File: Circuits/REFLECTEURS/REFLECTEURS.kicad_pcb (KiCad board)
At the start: 2 copper layers, 118.4 x 31 mm, 24 parts, among them P1 HE10-10, U1 3mm_hole, U2 3mm_hole

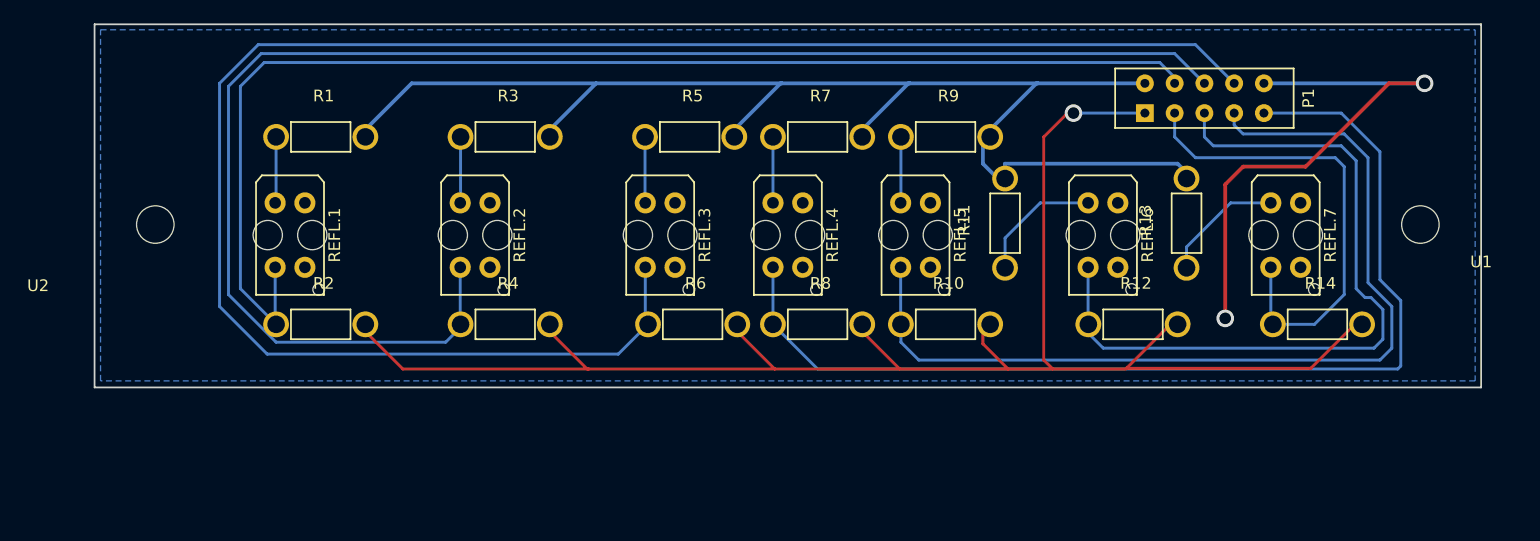
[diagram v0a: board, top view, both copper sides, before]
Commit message: Amelioration carte reflecteurs (simple face)
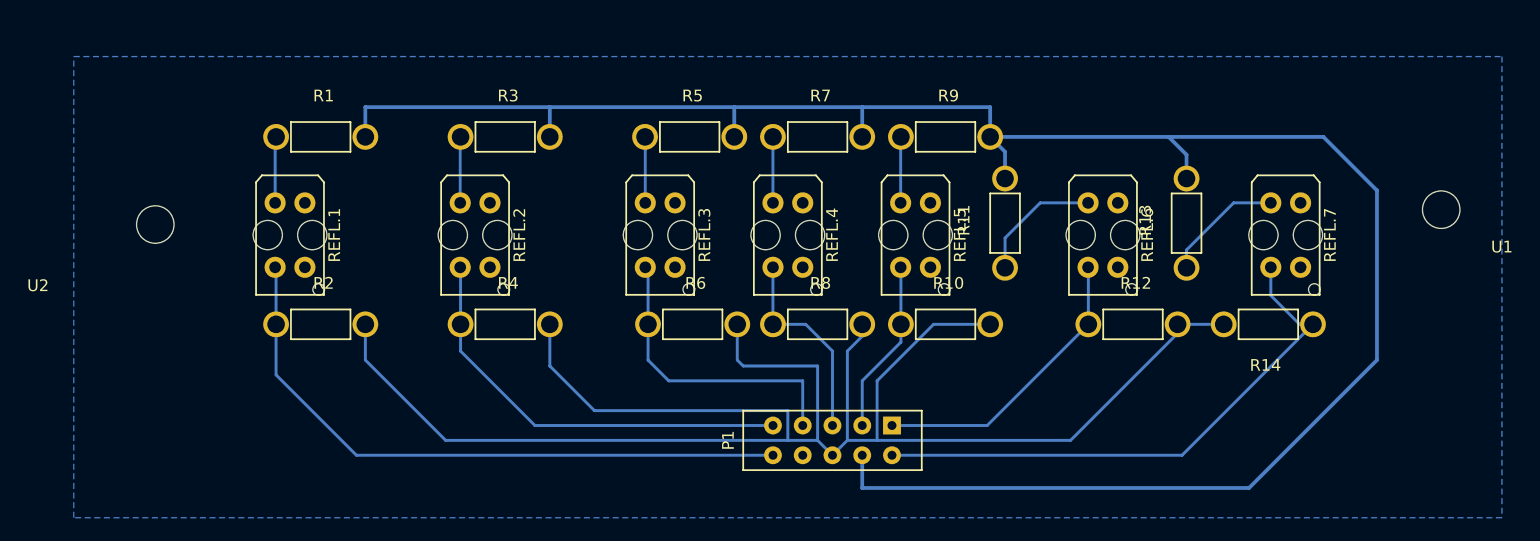
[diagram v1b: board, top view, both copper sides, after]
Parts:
- moved P1 43.1 mm to (86.4, 58.4), turned to 270 degrees
- moved R14 3.43 mm to (127.4, 48.5), turned to 180 degrees
- moved U1 2.18 mm to (143.5, 39.4)
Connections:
- P1 pad 1: +1V5 -> Net-(P1-Pad1)
- P1 pad 10: GND -> Net-(P1-Pad10)
- P1 pad 2: +5V -> Net-(P1-Pad2)
- P1 pad 4: Net-(P1-Pad4) -> +5V
- P1 pad 6: Net-(P1-Pad6) -> +1V5
- P1 pad 8: Net-(P1-Pad8) -> GND
- R10 pad 1: Net-(P1-Pad7) -> Net-(P1-Pad3)
- R12 pad 1: Net-(P1-Pad5) -> Net-(P1-Pad1)
- R14 pad 1: Net-(P1-Pad3) -> Net-(P1-Pad2)
- R2 pad 1: Net-(P1-Pad4) -> Net-(P1-Pad10)
- R4 pad 1: Net-(P1-Pad6) -> Net-(P1-Pad9)
- R6 pad 1: Net-(P1-Pad8) -> Net-(P1-Pad7)
- R8 pad 1: Net-(P1-Pad9) -> Net-(P1-Pad5)
- REFL.1 pad 2: Net-(P1-Pad4) -> Net-(P1-Pad10)
- REFL.2 pad 2: Net-(P1-Pad6) -> Net-(P1-Pad9)
- REFL.3 pad 2: Net-(P1-Pad8) -> Net-(P1-Pad7)
- REFL.4 pad 2: Net-(P1-Pad9) -> Net-(P1-Pad5)
- REFL.5 pad 2: Net-(P1-Pad7) -> Net-(P1-Pad3)
- REFL.6 pad 2: Net-(P1-Pad5) -> Net-(P1-Pad1)
- REFL.7 pad 2: Net-(P1-Pad3) -> Net-(P1-Pad2)
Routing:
- net Net-(P1-Pad8): track 152.7 -> 0.00 mm
- net Net-(P1-Pad6): track 130.5 -> 0.00 mm
- net Net-(P1-Pad4): track 108.1 -> 0.00 mm
- net +5V: track 119.3 -> 175.0 mm
- net Net-(P1-Pad10): track 0.00 -> 54.5 mm
- net Net-(P1-Pad9): track 90.4 -> 36.5 mm
- net Net-(P1-Pad7): track 80.1 -> 26.3 mm
- net Net-(P1-Pad2): track 0.00 -> 47.8 mm
- net Net-(P1-Pad5): track 63.9 -> 17.5 mm
- net GND: track 46.0 -> 0.00 mm, vias 2 -> 0
- net Net-(P1-Pad3): track 40.6 -> 14.9 mm
- net Net-(P1-Pad1): track 0.00 -> 25.2 mm
- net +1V5: track 144.1 -> 156.9 mm, vias 1 -> 0
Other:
- board outline removed

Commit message: Ameliorations cartes + rapport
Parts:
- moved R9 2.54 mm to (94.7, 32.5)
- moved R5 1.78 mm to (68.6, 32.5)
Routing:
- net +5V: track 175.0 -> 173.5 mm
- net Net-(R5-Pad1): track 5.64 -> 7.00 mm
- net Net-(R9-Pad1): track 5.64 -> 6.72 mm
